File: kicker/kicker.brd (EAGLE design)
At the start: 59.7 x 56.3 mm, 28 parts, among them T1 NPN_BC817,215, T2 NPN_BC817,215, T3 NPN_BC817,215, T4 NPN_BC817,215, X1 JST-XH-06-PIN-LONG-PAD

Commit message: details
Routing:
- net CAP: track 8.67 -> 9.33 mm
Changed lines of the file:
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@@
 <contactref element="R35" pad="2"/>
 <contactref element="X1" pad="6"/>
-<wire x1="56.134" y1="1.27" x2="52.004" y2="8.89" width="0.381" layer="1"/>
 <wire x1="47.178" y1="8.89" x2="52.004" y2="8.89" width="0" layer="19" extent="1-1"/>
+<wire x1="56.134" y1="1.27" x2="56.134" y2="4.76" width="0.4064" layer="1"/>
+<wire x1="56.134" y1="4.76" x2="52.004" y2="8.89" width="0.4064" layer="1"/>
 </signal>
 <signal name="BOOST_EN">

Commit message: rearranging rev0 board for 2 big moses
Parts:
- removed U$2, U$3: (no value), SparkFun-Hardware:STAND-OFF
- moved R8 46.5 mm to (20.6, 48.0), flipped to the bottom, turned to 0 degrees
- moved R33 44.3 mm to (15.2, 43.2), flipped to the bottom, turned to 90 degrees
- moved R6 39.9 mm to (13.0, 37.6), flipped to the bottom, turned to 90 degrees
- moved U$4 38.3 mm to (26.2, 45.5), flipped to the bottom
- moved T3 38.1 mm to (16.5, 38.6), flipped to the bottom, turned to 270 degrees
- moved R2 37.9 mm to (10.4, 37.6), flipped to the bottom, turned to 270 degrees
- moved T4 37.6 mm to (31.2, 44.2), flipped to the bottom, turned to 0 degrees
- moved R7 36.1 mm to (31.2, 48.0), flipped to the bottom, turned to 180 degrees
- moved R34 35.8 mm to (52.3, 44.2), flipped to the bottom, turned to 90 degrees
- moved T2 35.2 mm to (20.6, 44.5), flipped to the bottom, turned to 0 degrees
- moved R35 30.8 mm to (52.3, 39.6), flipped to the bottom, turned to 90 degrees
- moved R36 28.7 mm to (9.91, 42.7), flipped to the bottom, turned to 270 degrees
- moved BOOST_EN 28.7 mm to (2.54, 42.7)
- moved U$15 28.7 mm to (6.35, 42.7), flipped to the bottom, turned to 270 degrees
- moved R32 26.3 mm to (31.8, 37.8), flipped to the bottom, turned to 270 degrees
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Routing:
- net CAP: track 9.33 -> 44.7 mm, vias 0 -> 1
- net N$2: track 11.6 -> 18.2 mm
- net GND: track 52.6 -> 58.3 mm
- net N$36: track 11.4 -> 8.89 mm

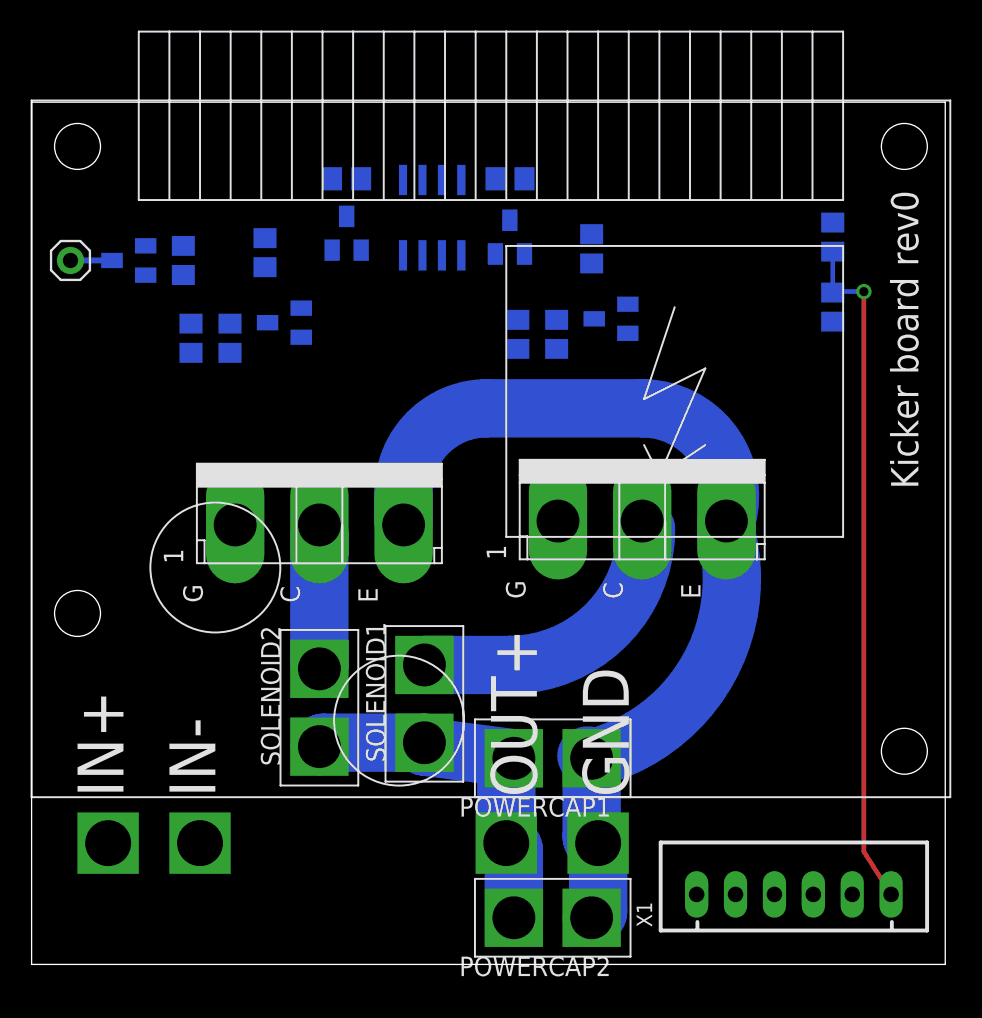
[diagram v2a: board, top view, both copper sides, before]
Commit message: Using mos driver on kicker board
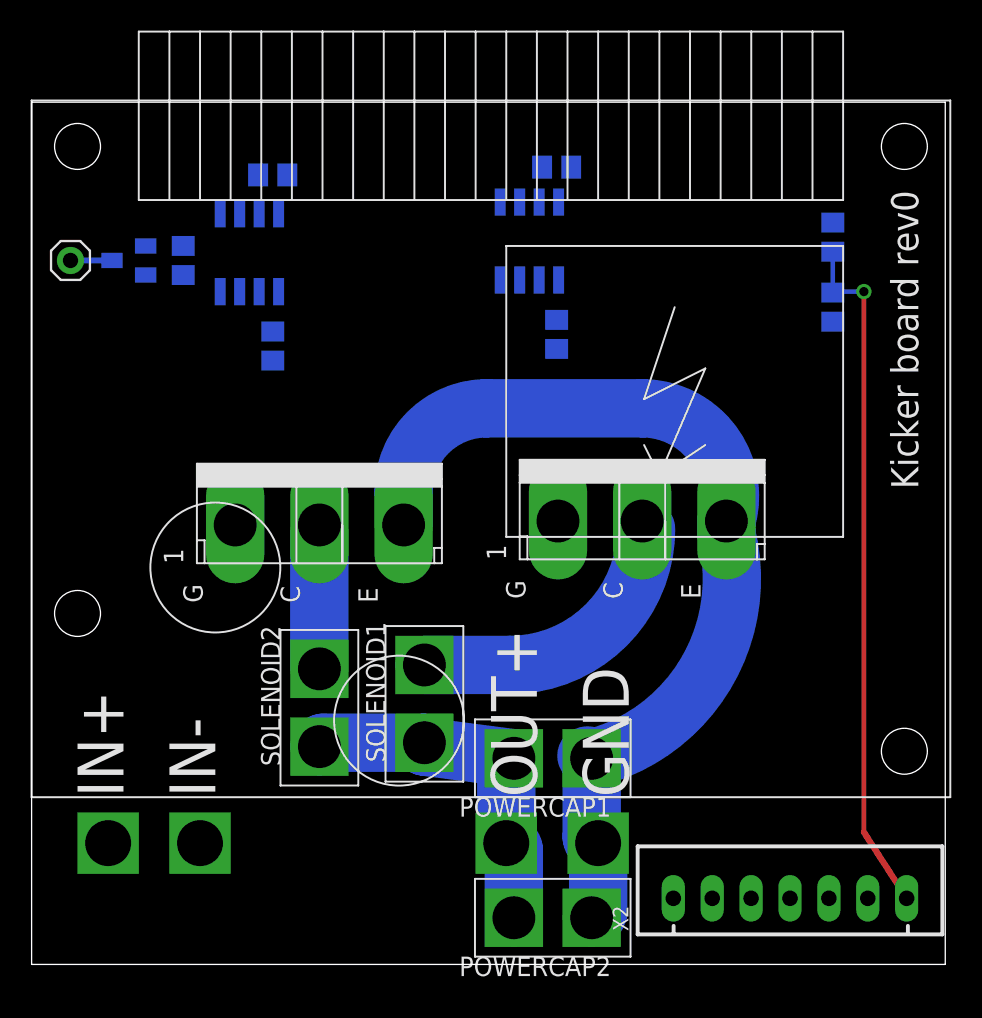
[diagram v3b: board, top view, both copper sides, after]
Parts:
- removed R3, R33, R7, R8: 3K, rhoban:R0805
- removed R32: 10K, rhoban:R0805
- removed T1, T2, T3, T4: NPN_BC817,215, rhoban:SOT-23
- removed U$4: ACPL-227-500E, rhoban:SO8
- removed X1: JST-XH-06-PIN-LONG-PAD, Rembrandt Electronics - JST XH Connectors v1-0:JST-XH-06-PACKAGE-LONG-PAD
- added DRV1, DRV2: OPEN-BLDC_IR2101, rhoban:OPEN-BLDC_SO-8
- added R1: 3K, rhoban:R0805
- added X2: JST-XH-07-PIN-LONG-PAD, Rembrandt Electronics - JST XH Connectors v1-0:JST-XH-07-PACKAGE-LONG-PAD
- R2: value 10K -> 3K
- R5, R6: value 1K -> 10
- moved R2 11.9 mm to (15.7, 48.3), turned to 180 degrees
- moved R6 2.84 mm to (15.7, 37.1)
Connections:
- removed net KICK1R: R7.1, T2.1, U$4.1
- removed net KICK2R: R8.1, T4.1, U$4.3
- removed net KICK_TR1: R2.1, T1.1, T2.3, U$4.8
- removed net KICK_TR2: R32.1, T3.1, T4.3, U$4.6
- removed net N$35: R33.1, R6.2, T3.3
- removed net N$4: R3.1, R5.2, T1.3
- new net 12V: DRV1.1, DRV2.1, X2.3
- new net N$1: DRV2.3, R2.1
- new net N$3: DRV2.5, R6.2
- new net N$5: DRV1.3, R1.1
- new net N$9: DRV1.5, R5.2
- net BOOST_EN: now also X2.4; no longer X1.3
- net CAP: now also X2.7; no longer X1.6
- net GND: now also DRV1.4, DRV2.4, X2.1; no longer T1.2, T2.2, T3.2, T4.2, U$4.2, U$4.4, U$4.5, U$4.7, X1.1
- net KICK1: now also R1.2, X2.5; no longer R7.2, X1.4
- net KICK2: now also R2.2, X2.6; no longer R8.2, X1.5
- net VIN: now also X2.2; no longer R2.2, R3.2, R32.2, R33.2, X1.2
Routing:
- net CAP: track 44.7 -> 45.2 mm

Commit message: kicker board routed
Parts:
- added C1, C2: (no value), rcl:C0805
- added D1, D5: (no value), diode:SOD80C
- added D2, D3: 1N6267A, diode:C4111-15
- added D4: RED, SparkFun:LED-1206
- added Q1, Q2: BSS123, transistor-small-signal:SOT23
- added R10, R11, R9: 10K, rhoban:R0805
- added R3: 1M, rhoban:R0805
- added R4, R7, R8: 3K, rhoban:R0805
- R34: value 2M -> 1M
- moved R35 31.8 mm to (52.6, 7.87), flipped to the top
- moved R34 31.0 mm to (50.8, 13.2), flipped to the top
- moved SOLENOID1 19.8 mm to (45.0, 15.7), turned to 180 degrees
- moved R1 19.0 mm to (49.0, 36.8)
- moved POWERCAP2 16.5 mm to (31.0, 15.2), turned to 270 degrees
- moved R2 16.0 mm to (26.9, 36.8)
- moved POWERCAP1 13.4 mm to (24.1, 15.2), turned to 270 degrees
- moved DRV1 11.0 mm to (42.2, 38.6), turned to 270 degrees
- moved DRV2 8.10 mm to (20.3, 37.8), turned to 270 degrees
- moved SOLENOID2 5.36 mm to (16.0, 15.5), turned to 180 degrees
- moved U$1 4.19 mm to (40.9, 29.7)
- moved R36 4.10 mm to (13.7, 44.2), turned to 180 degrees
- moved U$11 4.10 mm to (19.3, 29.5)
- moved R6 2.05 mm to (14.0, 36.1), turned to 180 degrees
- moved R5 1.63 mm to (35.3, 36.6), turned to 180 degrees
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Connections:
- new net N$10: Q2.2, R9.2
- new net N$11: D4.A, R9.1
- new net N$12: Q1.2, Q2.3
- new net N$13: DRV1.2, R7.1
- new net N$14: Q1.1, R10.1, R11.2
- new net N$16: D5.C, Q2.1, R11.1
- new net N$4: R3.1, R34.2
- new net N$6: DRV2.2, R4.1
- net 12V: now also C1.1, C2.1, DRV1.8, DRV2.8
- net CAP: now also D1.C
- net GND: now also C1.2, C2.2, D1.A, D4.C, D5.A, DRV1.6, DRV2.6, R4.2, R7.2, R8.2
- net N$2: now also D2.A
- net N$36: now also D3.A
- net N$38: now also R8.1
- net VBOOST: now also D2.C, D3.C, Q1.3, R10.2, R3.2; no longer R34.2
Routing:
- net GND: track 58.3 -> 278.7 mm, vias 0 -> 45
- net 12V: track 0.00 -> 97.1 mm
- net BOOST_EN: track 0.00 -> 86.5 mm
- net KICK2: track 0.00 -> 85.3 mm, vias 0 -> 2
- net VBOOST: track 23.9 -> 81.7 mm
- net KICK1: track 0.00 -> 44.4 mm, vias 0 -> 2
- net CAP: track 45.2 -> 15.8 mm, vias 1 -> 0
- net N$36: track 8.89 -> 17.9 mm
- net N$11: track 0.00 -> 8.60 mm, vias 0 -> 1
- net N$7: track 0.00 -> 7.76 mm
- net N$38: track 0.00 -> 7.49 mm
- net N$8: track 0.00 -> 6.98 mm
- net N$14: track 0.00 -> 5.96 mm
- net N$16: track 0.00 -> 5.34 mm
- net N$2: track 18.2 -> 22.4 mm
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- added copper zone on layer 1, net GND
- added copper zone on layer 16, net GND
- added copper zone on layer 1, net N$2
- added copper zone on layer 1, net N$36
- added copper zone on layer 1, net VBOOST
- added copper zone on layer 1, net VIN
